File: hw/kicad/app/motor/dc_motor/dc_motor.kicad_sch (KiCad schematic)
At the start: 23 parts, among them J1 TOP, J2 Motor 1, J3 Motor 2, J4 Motor 3, J6 BOTTUM, U1 DRV8870DDA, U2 DRV8870DDA, U3 DRV8870DDA

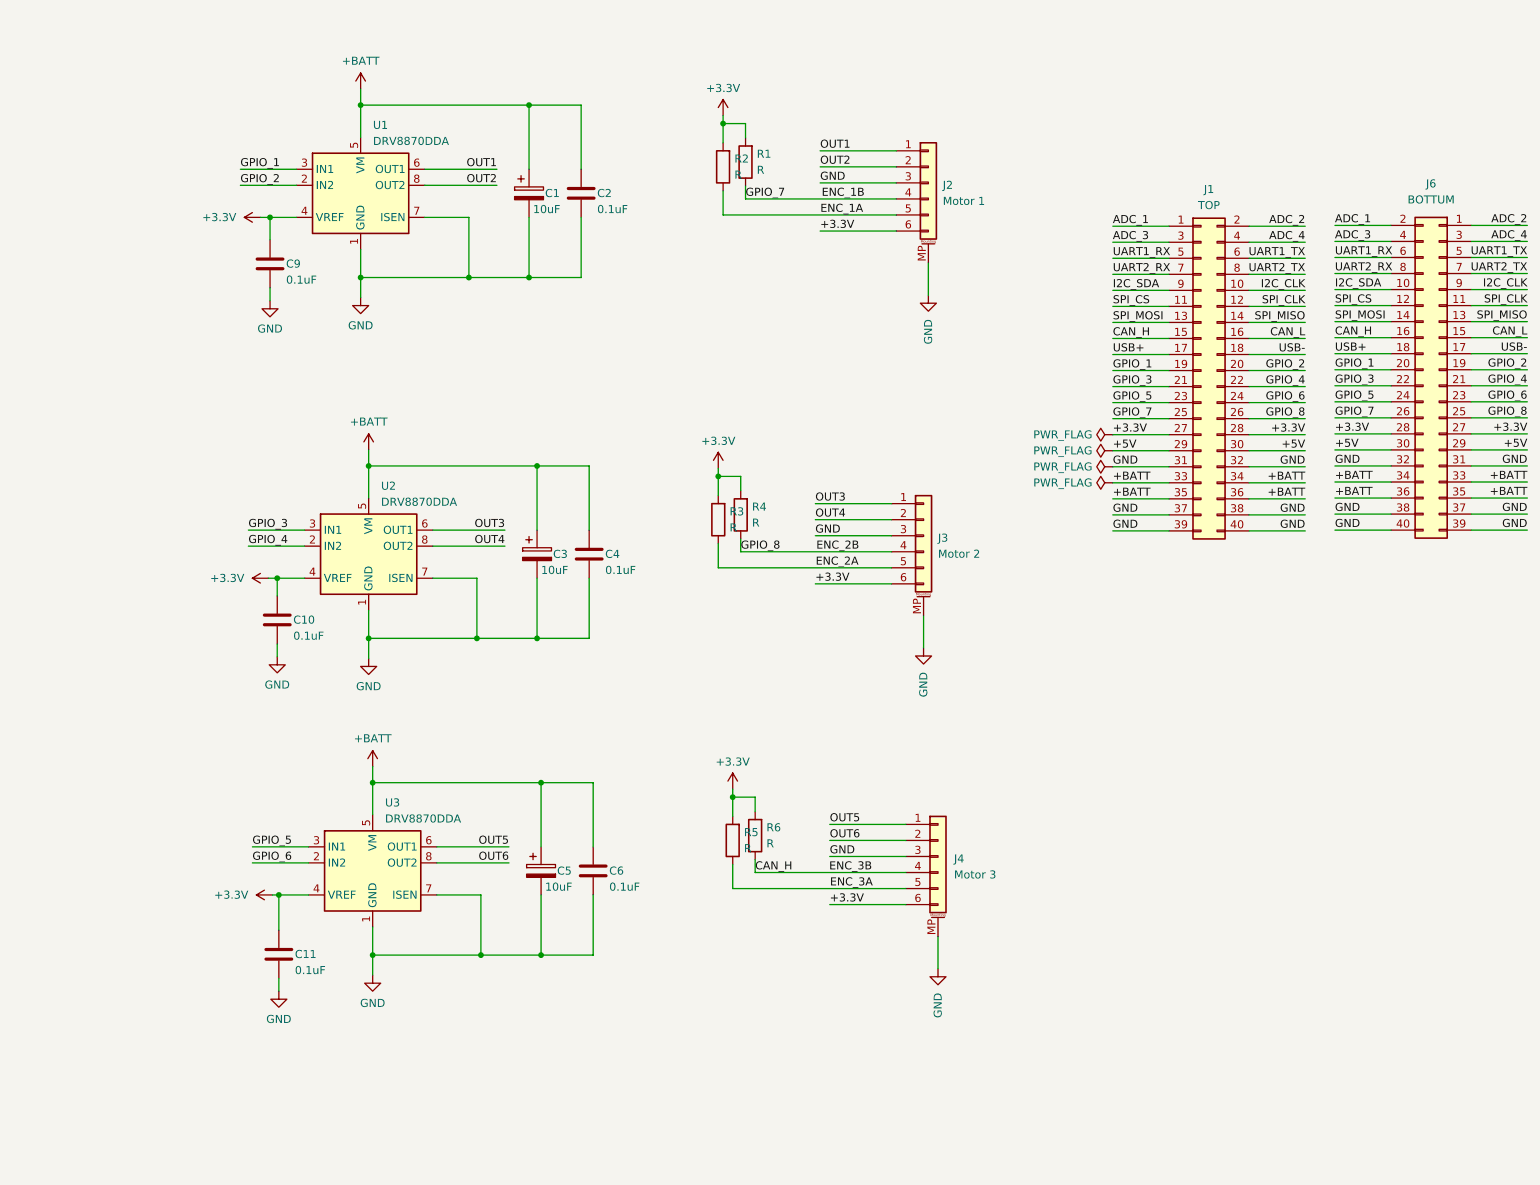
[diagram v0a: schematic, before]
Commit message: 更新dc motor板
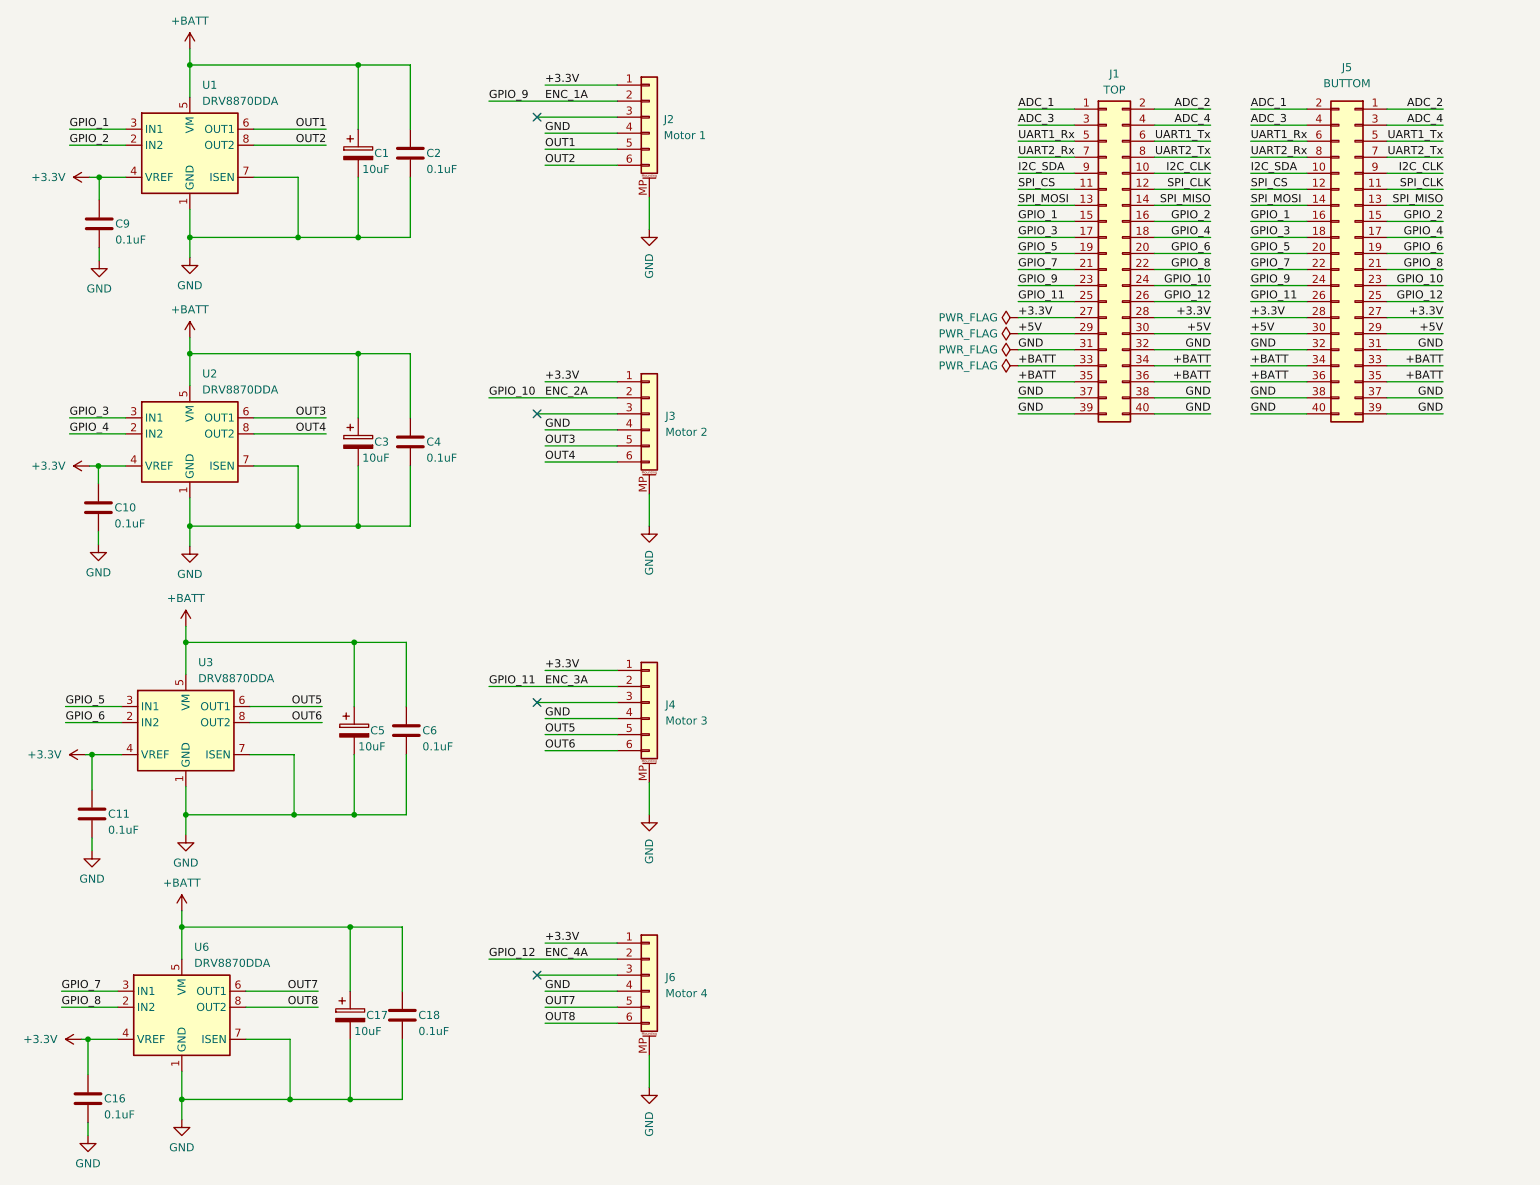
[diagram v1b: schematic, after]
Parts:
- removed J6: BOTTUM, Connector_PinHeader_1.27mm:PinHeader_2x20_P1.27mm_Vertical_SMD, symbol Connector_Generic:Conn_02x20_Odd_Even
- removed R1, R2, R3, R4, R5, R6: R, Resistor_SMD:R_0805_2012Metric, symbol Device:R
- added C16, C18: 0.1uF, Capacitor_SMD:C_0805_2012Metric, symbol Device:C
- added C17: 10uF, Capacitor_SMD:CP_Elec_6.3x5.4, symbol Device:C_Polarized
- added J5: BUTTOM, Connector_PinHeader_1.27mm:PinHeader_2x20_P1.27mm_Vertical_SMD, symbol Connector_Generic:Conn_02x20_Odd_Even
- added J6: Motor 4, Connector_JST:JST_GH_SM06B-GHS-TB_1x06-1MP_P1.25mm_Horizontal, symbol Connector_Generic_MountingPin:Conn_01x06_MountingPin
- added U6: DRV8870DDA, Package_SO:Texas_HTSOP-8-1EP_3.9x4.9mm_P1.27mm_EP2.95x4.9mm_Mask2.4x3.1mm_ThermalVias, symbol Driver_Motor:DRV8870DDA
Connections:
- net CAN_L is gone; now on net GPIO_2: J1.16 (Pin_16)
- net USB+ is gone; now on net GPIO_3: J1.17 (Pin_17)
- net USB- is gone; now on net GPIO_4: J1.18 (Pin_18)
- net +3.3V: now also J2.1 (Pin_1), J3.1 (Pin_1), J4.1 (Pin_1), C16.1, J5.27 (Pin_27), J5.28 (Pin_28), J6.1 (Pin_1), U6.4 (VREF); no longer J2.6 (Pin_6), J3.6 (Pin_6), J4.6 (Pin_6)
- net +5V: now also J5.29 (Pin_29), J5.30 (Pin_30)
- net +BATT: now also C17.1, C18.1, J5.33 (Pin_33), J5.34 (Pin_34), J5.35 (Pin_35), J5.36 (Pin_36), U6.5 (VM)
- net ADC_1: now also J5.2 (Pin_2)
- net ADC_2: now also J5.1 (Pin_1)
- net ADC_3: now also J5.4 (Pin_4)
- net ADC_4: now also J5.3 (Pin_3)
- net ENC_1A: now also J1.23 (Pin_23), J2.2 (Pin_2), J5.24 (Pin_24); no longer J2.5 (Pin_5)
- net ENC_2A: now also J1.24 (Pin_24), J3.2 (Pin_2), J5.23 (Pin_23); no longer J3.5 (Pin_5)
- net ENC_3A: now also J1.25 (Pin_25), J4.2 (Pin_2), J5.26 (Pin_26); no longer J4.5 (Pin_5)
- net GND: now also J2.4 (Pin_4), J3.4 (Pin_4), J4.4 (Pin_4), C16.2, C17.2, C18.2, J5.31 (Pin_31), J5.32 (Pin_32), J5.37 (Pin_37), J5.38 (Pin_38), J5.39 (Pin_39), J5.40 (Pin_40), J6.4 (Pin_4), J6.MP (MountPin), U6.1 (GND), U6.7 (ISEN), U6.9 (GND); no longer J2.3 (Pin_3), J3.3 (Pin_3), J4.3 (Pin_3)
- net GPIO_1: now also J1.15 (Pin_15), J5.16 (Pin_16); no longer J1.19 (Pin_19)
- net GPIO_2: now also J5.15 (Pin_15); no longer J1.20 (Pin_20)
- net GPIO_3: now also J5.18 (Pin_18); no longer J1.21 (Pin_21)
- net GPIO_4: now also J5.17 (Pin_17); no longer J1.22 (Pin_22)
- net GPIO_5: now also J1.19 (Pin_19), J5.20 (Pin_20); no longer J1.23 (Pin_23)
- net GPIO_6: now also J1.20 (Pin_20), J5.19 (Pin_19); no longer J1.24 (Pin_24)
- net I2C_CLK: now also J5.9 (Pin_9)
- net I2C_SDA: now also J5.10 (Pin_10)
- net OUT1: now also J2.5 (Pin_5); no longer J2.1 (Pin_1)
- net OUT2: now also J2.6 (Pin_6); no longer J2.2 (Pin_2)
- net OUT3: now also J3.5 (Pin_5); no longer J3.1 (Pin_1)
- net OUT4: now also J3.6 (Pin_6); no longer J3.2 (Pin_2)
- net OUT5: now also J4.5 (Pin_5); no longer J4.1 (Pin_1)
- net OUT6: now also J4.6 (Pin_6); no longer J4.2 (Pin_2)
- net SPI_CLK: now also J5.11 (Pin_11)
- net SPI_CS: now also J5.12 (Pin_12)
- net SPI_MISO: now also J5.13 (Pin_13)
- net SPI_MOSI: now also J5.14 (Pin_14)
- removed net CAN_H: J1.15 (Pin_15), J4.4 (Pin_4)
- removed net ENC_1B: J1.25 (Pin_25), J2.4 (Pin_4)
- net ENC_2B renamed ENC_4A
- net ENC_4A: now also J5.25 (Pin_25), J6.2 (Pin_2); no longer J3.4 (Pin_4)
- net UART1_RX renamed UART1_Rx
- net UART1_Rx: now also J5.6 (Pin_6)
- net UART1_TX renamed UART1_Tx
- net UART1_Tx: now also J5.5 (Pin_5)
- net UART2_RX renamed UART2_Rx
- net UART2_Rx: now also J5.8 (Pin_8)
- net UART2_TX renamed UART2_Tx
- net UART2_Tx: now also J5.7 (Pin_7)
- new net GPIO_7: J1.21 (Pin_21), J5.22 (Pin_22), U6.3 (IN1)
- new net GPIO_8: J1.22 (Pin_22), J5.21 (Pin_21), U6.2 (IN2)
- new net OUT7: J6.5 (Pin_5), U6.6 (OUT1)
- new net OUT8: J6.6 (Pin_6), U6.8 (OUT2)
- no-connect marks 0 -> 4
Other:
- moved on the sheet: C1, C10, C11, C2, C3, C4, C5, C6, C9, J2, U1, U2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
